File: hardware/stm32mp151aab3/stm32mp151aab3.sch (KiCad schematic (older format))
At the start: 1 part

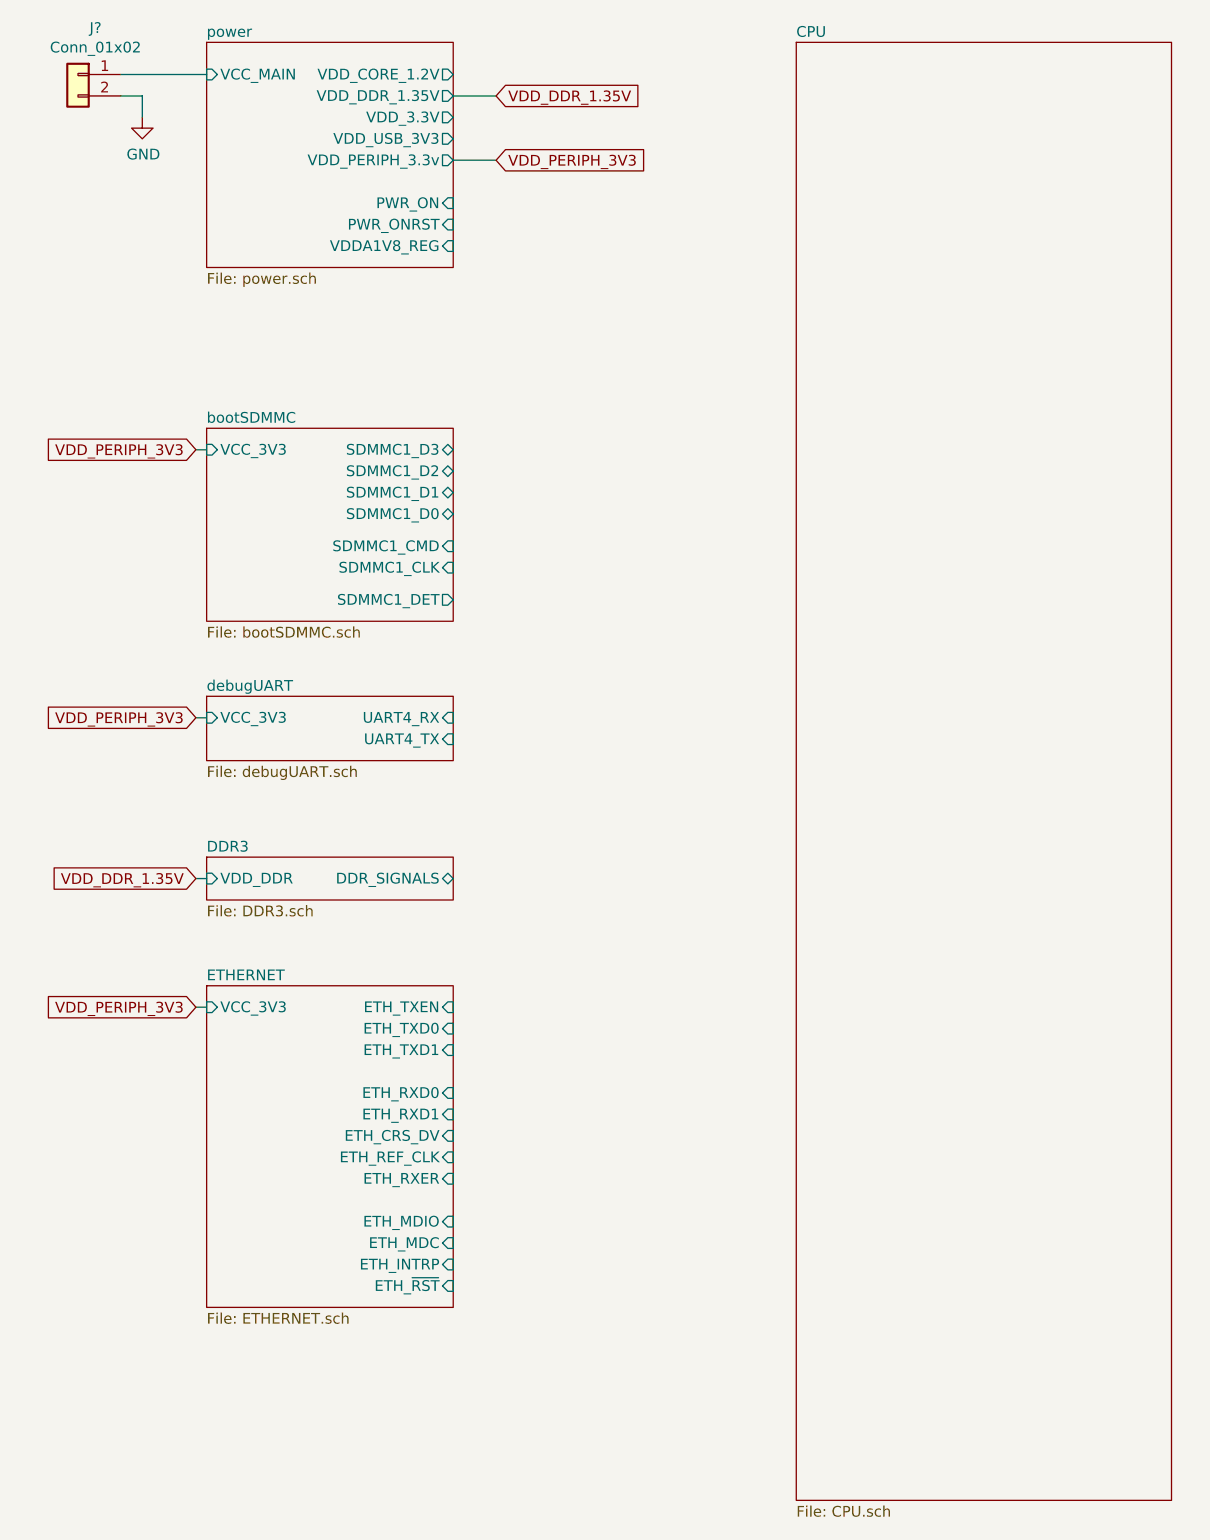
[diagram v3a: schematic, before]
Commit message: update schematic and pdf
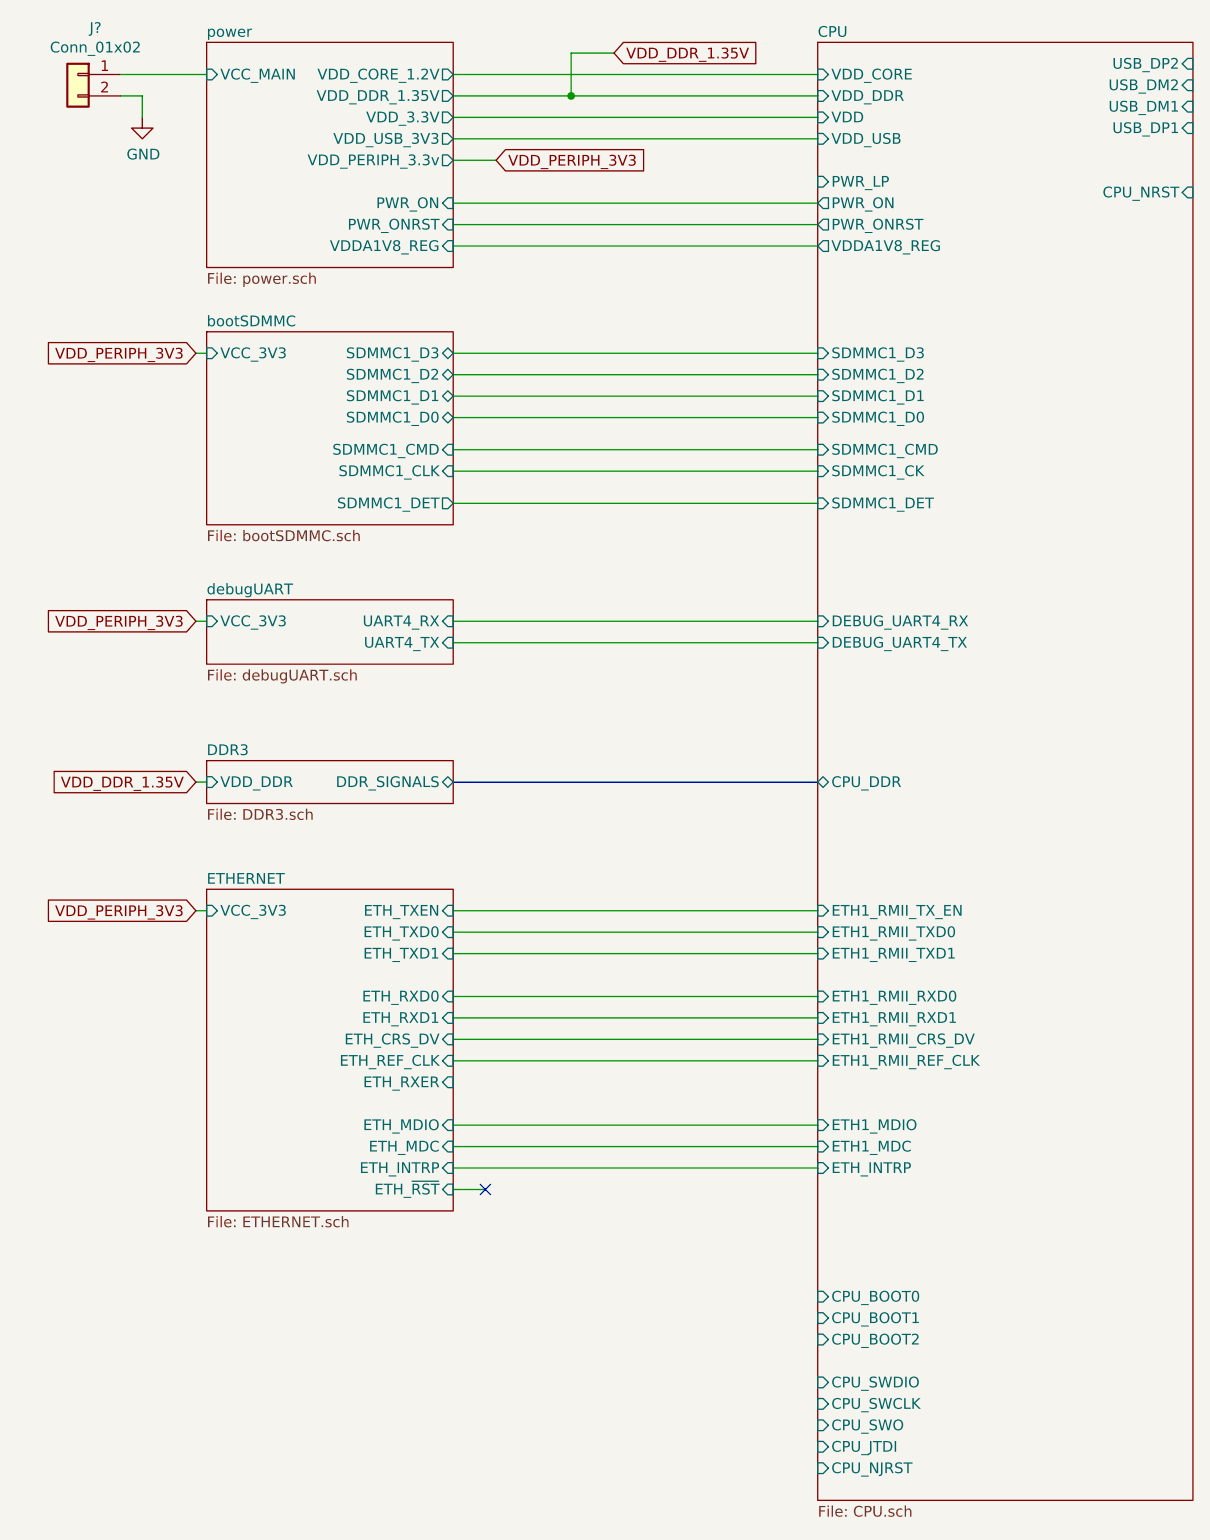
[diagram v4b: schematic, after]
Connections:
- no-connect marks 0 -> 1
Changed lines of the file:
@@
 $EndSheet
 $Sheet
-S 1250 3650 1150 300
+S 1250 3200 1150 300
 U 5FE704D9
 F0 "debugUART" 50
 F1 "debugUART.sch" 50
-F2 "VCC_3V3" I L 1250 3750 50
-F3 "UART4_RX" I R 2400 3750 50
-F4 "UART4_TX" I R 2400 3850 50
+F2 "VCC_3V3" I L 1250 3300 50
+F3 "UART4_RX" I R 2400 3300 50
+F4 "UART4_TX" I R 2400 3400 50
 $EndSheet
 Text GLabel 2600 1150 2    50   Input ~ 0
@@
 	2600 1150 2400 1150
 Wire Wire Line
-	1200 2500 1250 2500
-Text GLabel 1200 2500 0    50   Input ~ 0
-VDD_PERIPH_3V3
-$Sheet
-S 1250 2400 1150 900
+	1200 2050 1250 2050
+Text GLabel 1200 2050 0    50   Input ~ 0
+VDD_PERIPH_3V3
+$Sheet
+S 1250 1950 1150 900
 U 5FE7045F
 F0 "bootSDMMC" 50
 F1 "bootSDMMC.sch" 50
-F2 "VCC_3V3" I L 1250 2500 50
-F3 "SDMMC1_D2" B R 2400 2600 50
-F4 "SDMMC1_D3" B R 2400 2500 50
-F5 "SDMMC1_CMD" I R 2400 2950 50
-F6 "SDMMC1_CLK" I R 2400 3050 50
-F7 "SDMMC1_D0" B R 2400 2800 50
-F8 "SDMMC1_D1" B R 2400 2700 50
-F9 "SDMMC1_DET" O R 2400 3200 50
-$EndSheet
-Text GLabel 1200 3750 0    50   Input ~ 0
-VDD_PERIPH_3V3
-Wire Wire Line
-	1200 3750 1250 3750
-$Sheet
-S 4000 600  1750 6800
-U 5FE97965
-F0 "CPU" 50
-F1 "CPU.sch" 50
-$EndSheet
-$Sheet
-S 1250 4400 1150 200
+F2 "VCC_3V3" I L 1250 2050 50
+F3 "SDMMC1_D2" B R 2400 2150 50
+F4 "SDMMC1_D3" B R 2400 2050 50
+F5 "SDMMC1_CMD" I R 2400 2500 50
+F6 "SDMMC1_CLK" I R 2400 2600 50
+F7 "SDMMC1_D0" B R 2400 2350 50
+F8 "SDMMC1_D1" B R 2400 2250 50
+F9 "SDMMC1_DET" O R 2400 2750 50
+$EndSheet
+Text GLabel 1200 3300 0    50   Input ~ 0
+VDD_PERIPH_3V3
+Wire Wire Line
+	1200 3300 1250 3300
+$Sheet
+S 1250 3950 1150 200
 U 5FEB1357
 F0 "DDR3" 50
 F1 "DDR3.sch" 50
-F2 "VDD_DDR" I L 1250 4500 50
-F3 "DDR_SIGNALS" B R 2400 4500 50
-$EndSheet
-Text GLabel 2600 850  2    50   Input ~ 0
+F2 "VDD_DDR" I L 1250 4050 50
+F3 "DDR_SIGNALS" B R 2400 4050 50
+$EndSheet
+Text GLabel 3150 650  2    50   Input ~ 0
 VDD_DDR_1.35V
-Wire Wire Line
-	2600 850  2400 850
-Text GLabel 1200 4500 0    50   Input ~ 0
+Text GLabel 1200 4050 0    50   Input ~ 0
 VDD_DDR_1.35V
 Wire Wire Line
-	1200 4500 1250 4500
+	1200 4050 1250 4050
 $Comp
 L Connector_Generic:Conn_01x02 J?
@@
 	1250 750  850  750
 $Sheet
-S 1250 5000 1150 1500
+S 1250 4550 1150 1500
 U 60175391
 F0 "ETHERNET" 50
 F1 "ETHERNET.sch" 50
-F2 "VCC_3V3" I L 1250 5100 50
-F3 "ETH_TXEN" I R 2400 5100 50
-F4 "ETH_TXD0" I R 2400 5200 50
-F5 "ETH_TXD1" I R 2400 5300 50
-F6 "ETH_RXD0" I R 2400 5500 50
-F7 "ETH_RXD1" I R 2400 5600 50
-F8 "ETH_CRS_DV" I R 2400 5700 50
-F9 "ETH_REF_CLK" I R 2400 5800 50
-F10 "ETH_RXER" I R 2400 5900 50
-F11 "ETH_MDIO" I R 2400 6100 50
-F12 "ETH_MDC" I R 2400 6200 50
-F13 "ETH_INTRP" I R 2400 6300 50
-F14 "ETH_~RST" I R 2400 6400 50
-$EndSheet
-Text GLabel 1200 5100 0    50   Input ~ 0
-VDD_PERIPH_3V3
-Wire Wire Line
-	1200 5100 1250 5100
+F2 "VCC_3V3" I L 1250 4650 50
+F3 "ETH_TXEN" I R 2400 4650 50
+F4 "ETH_TXD0" I R 2400 4750 50
+F5 "ETH_TXD1" I R 2400 4850 50
+F6 "ETH_RXD0" I R 2400 5050 50
+F7 "ETH_RXD1" I R 2400 5150 50
+F8 "ETH_CRS_DV" I R 2400 5250 50
+F9 "ETH_REF_CLK" I R 2400 5350 50
+F10 "ETH_RXER" I R 2400 5450 50
+F11 "ETH_MDIO" I R 2400 5650 50
+F12 "ETH_MDC" I R 2400 5750 50
+F13 "ETH_INTRP" I R 2400 5850 50
+F14 "ETH_~RST" I R 2400 5950 50
+$EndSheet
+Text GLabel 1200 4650 0    50   Input ~ 0
+VDD_PERIPH_3V3
+Wire Wire Line
+	1200 4650 1250 4650
+Wire Wire Line
+	2400 1550 4100 1550
+Wire Wire Line
+	2400 1350 4100 1350
+Wire Wire Line
+	4100 1450 2400 1450
+Wire Wire Line
+	2400 750  4100 750
+Wire Wire Line
+	2400 1050 4100 1050
+Wire Wire Line
+	2400 950  4100 950
+Wire Wire Line
+	2400 850  2950 850
+Wire Wire Line
+	3150 650  2950 650
+Wire Wire Line
+	2950 650  2950 850
+Connection ~ 2950 850
+Wire Wire Line
+	2950 850  4100 850
+Wire Bus Line
+	2400 4050 4100 4050
+Wire Wire Line
+	2400 3300 4100 3300
+Wire Wire Line
+	4100 3400 2400 3400
+Wire Wire Line
+	4100 2050 2400 2050
+Wire Wire Line
+	4100 2150 2400 2150
+Wire Wire Line
+	2400 2250 4100 2250
+Wire Wire Line
+	4100 2350 2400 2350
+Wire Wire Line
+	2400 2500 4100 2500
+Wire Wire Line
+	4100 2600 2400 2600
+Wire Wire Line
+	2400 2750 4100 2750
+$Sheet
+S 4100 600  1750 6800
+U 5FE97965
+F0 "CPU" 50
+F1 "CPU.sch" 50
+F2 "VDD_CORE" I L 4100 750 50
+F3 "VDD" I L 4100 950 50
+F4 "PWR_LP" I L 4100 1250 50
+F5 "CPU_BOOT0" I L 4100 6450 50
+F6 "CPU_BOOT1" I L 4100 6550 50
+F7 "CPU_BOOT2" I L 4100 6650 50
+F8 "VDD_USB" I L 4100 1050 50
+F9 "USB_DP2" I R 5850 700 50
+F10 "USB_DM2" I R 5850 800 50
+F11 "USB_DM1" I R 5850 900 50
+F12 "USB_DP1" I R 5850 1000 50
+F13 "CPU_NRST" I R 5850 1300 50
+F14 "VDDA1V8_REG" O L 4100 1550 50
+F15 "PWR_ON" O L 4100 1350 50
+F16 "PWR_ONRST" O L 4100 1450 50
+F17 "VDD_DDR" I L 4100 850 50
+F18 "CPU_SWDIO" I L 4100 6850 50
+F19 "CPU_SWCLK" I L 4100 6950 50
+F20 "CPU_SWO" I L 4100 7050 50
+F21 "CPU_JTDI" I L 4100 7150 50
+F22 "CPU_NJRST" I L 4100 7250 50
+F23 "CPU_DDR" B L 4100 4050 50
+F24 "DEBUG_UART4_RX" I L 4100 3300 50
+F25 "DEBUG_UART4_TX" I L 4100 3400 50
+F26 "SDMMC1_CK" I L 4100 2600 50
+F27 "SDMMC1_CMD" I L 4100 2500 50
+F28 "SDMMC1_D0" I L 4100 2350 50
+F29 "SDMMC1_D1" I L 4100 2250 50
+F30 "SDMMC1_D2" I L 4100 2150 50
+F31 "SDMMC1_D3" I L 4100 2050 50
+F32 "SDMMC1_DET" I L 4100 2750 50
+F33 "ETH1_RMII_REF_CLK" I L 4100 5350 50
+F34 "ETH1_MDIO" I L 4100 5650 50
+F35 "ETH1_RMII_CRS_DV" I L 4100 5250 50
+F36 "ETH1_RMII_TX_EN" I L 4100 4650 50
+F37 "ETH1_RMII_TXD0" I L 4100 4750 50
+F38 "ETH1_RMII_TXD1" I L 4100 4850 50
+F39 "ETH1_MDC" I L 4100 5750 50
+F40 "ETH1_RMII_RXD0" I L 4100 5050 50
+F41 "ETH1_RMII_RXD1" I L 4100 5150 50
+F42 "ETH_INTRP" I L 4100 5850 50
+$EndSheet
+Wire Wire Line
+	4100 5350 2400 5350
+Wire Wire Line
+	4100 5650 2400 5650
+Wire Wire Line
+	4100 5250 2400 5250
+Wire Wire Line
+	2400 4650 4100 4650
+Wire Wire Line
+	4100 5750 2400 5750
+Wire Wire Line
+	4100 4750 2400 4750
+Wire Wire Line
+	4100 4850 2400 4850
+Wire Wire Line
+	4100 5050 2400 5050
+Wire Wire Line
+	2400 5150 4100 5150
+Wire Wire Line
+	4100 5850 2400 5850
+Wire Wire Line
+	2400 5950 2550 5950
+NoConn ~ 2550 5950
 $EndSCHEMATC
